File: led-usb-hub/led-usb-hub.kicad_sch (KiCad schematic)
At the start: 142 parts, among them J1 USBC_USB2.0, J2 RGBUSB_54-00266, J3 RGBUSB_54-00266, J4 RGBUSB_54-00266, J5 SWD, SW1 RESET, SW2 BOOLSEL, SW3 LED_EN, U1 RP2040, U10 TPD2EUSB30, U11 TPD2EUSB30, U12 TC54VN3002, U13 W25Q16JVSN, U2 TPS2042D, U3 TPS2042D, U4 TPS563257DRLR, U5 TPS563257DRLR, U6 TUSB2046IBVF, U7 TPD2EUSB30, U8 TPD2EUSB30, U9 TPD2EUSB30, Y1 12Mhz, Y2 6Mhz

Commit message: Even more goddamn clean up and closer placement of decoupling caps
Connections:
- net EN_LED: now also U1.31 (GPIO20); no longer U1.32 (GPIO21)
- net LED_PWR: now also U1.36 (GPIO24); no longer U1.37 (GPIO25)
- net LED_USB: now also U1.35 (GPIO23); no longer U1.36 (GPIO24)
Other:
- moved on the sheet: R52, SW3
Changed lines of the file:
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@@
   (junction (at 33.02 82.55) (diameter 0) (color 0 0 0 0)
   )
-  (junction (at 299.72 243.84) (diameter 0) (color 0 0 0 0)
+  (junction (at 299.72 241.3) (diameter 0) (color 0 0 0 0)
   )
   (junction (at 158.75 146.05) (diameter 0) (color 0 0 0 0)
@@
   (no_connect (at 281.94 210.82))
   (no_connect (at 281.94 236.22))
-  (no_connect (at 281.94 248.92))
+  (no_connect (at 281.94 254))
   (no_connect (at 247.65 90.17))
   (no_connect (at 281.94 208.28))
-  (no_connect (at 281.94 241.3))
+  (no_connect (at 281.94 243.84))
   (bus_entry (at 360.68 199.39) (size -2.54 2.54)
     (stroke (width 0) (type default))
@@
     (stroke (width 0) (type default))
   )
-  (wire (pts (xy 299.72 243.84) (xy 304.8 243.84))
+  (wire (pts (xy 299.72 241.3) (xy 304.8 241.3))
     (stroke (width 0) (type default))
   )
@@
     (stroke (width 0) (type default))
   )
-  (wire (pts (xy 281.94 243.84) (xy 299.72 243.84))
+  (wire (pts (xy 281.94 241.3) (xy 299.72 241.3))
     (stroke (width 0) (type default))
   )
@@
     (stroke (width 0) (type default))
   )
-  (wire (pts (xy 284.48 254) (xy 281.94 254))
+  (wire (pts (xy 284.48 251.46) (xy 281.94 251.46))
     (stroke (width 0) (type default))
   )
@@
     (stroke (width 0) (type default))
   )
-  (wire (pts (xy 299.72 241.3) (xy 299.72 243.84))
+  (wire (pts (xy 299.72 238.76) (xy 299.72 241.3))
     (stroke (width 0) (type default))
   )
@@
     (stroke (width 0) (type default))
   )
-  (wire (pts (xy 299.72 233.68) (xy 299.72 231.14))
+  (wire (pts (xy 299.72 231.14) (xy 299.72 228.6))
     (stroke (width 0) (type default))
   )
@@
     (stroke (width 0) (type default))
   )
-  (wire (pts (xy 284.48 251.46) (xy 281.94 251.46))
+  (wire (pts (xy 284.48 248.92) (xy 281.94 248.92))
     (stroke (width 0) (type default))
   )
@@
     (stroke (width 0) (type default))
   )
-  (wire (pts (xy 314.96 243.84) (xy 320.04 243.84))
+  (wire (pts (xy 314.96 241.3) (xy 320.04 241.3))
     (stroke (width 0) (type default))
   )
@@
     (stroke (width 0) (type default))
   )
-  (wire (pts (xy 320.04 243.84) (xy 320.04 247.65))
+  (wire (pts (xy 320.04 241.3) (xy 320.04 245.11))
     (stroke (width 0) (type default))
   )
@@
     (effects (font (size 1.27 1.27) (color 0 0 194 0)) (justify right bottom))
   )
-  (label "EN_LED" (at 299.72 243.84 180) (fields_autoplaced)
+  (label "EN_LED" (at 299.72 241.3 180) (fields_autoplaced)
     (effects (font (size 1.27 1.27) (color 0 0 194 0)) (justify right bottom))
   )
@@
     )
   )
-  (global_label "LED_USB" (shape output) (at 284.48 251.46 0) (fields_autoplaced)
+  (global_label "LED_USB" (shape output) (at 284.48 248.92 0) (fields_autoplaced)
     (effects (font (size 1.27 1.27)) (justify left))
-    (property "Intersheetrefs" "${INTERSHEET_REFS}" (at 295.6105 251.46 0)
+    (property "Intersheetrefs" "${INTERSHEET_REFS}" (at 295.6105 248.92 0)
       (effects (font (size 1.27 1.27)) (justify left) hide)
     )
@@
     )
   )
-  (global_label "LED_PWR" (shape output) (at 284.48 254 0) (fields_autoplaced)
+  (global_label "LED_PWR" (shape output) (at 284.48 251.46 0) (fields_autoplaced)
     (effects (font (size 1.27 1.27)) (justify left))
-    (property "Intersheetrefs" "${INTERSHEET_REFS}" (at 295.7919 254 0)
+    (property "Intersheetrefs" "${INTERSHEET_REFS}" (at 295.7919 251.46 0)
       (effects (font (size 1.27 1.27)) (justify left) hide)
     )
@@
     )
   )
-  (symbol (lib_id "Switch:SW_Push") (at 309.88 243.84 0) (unit 1)
+  (symbol (lib_id "Switch:SW_Push") (at 309.88 241.3 0) (unit 1)
     (in_bom yes) (on_board yes) (dnp no)
-    (property "Reference" "SW3" (at 309.88 246.38 0)
+    (property "Reference" "SW3" (at 309.88 243.84 0)
       (effects (font (size 1.27 1.27)))
     )
-    (property "Value" "LED_EN" (at 309.88 248.92 0)
+    (property "Value" "LED_EN" (at 309.88 246.38 0)
       (effects (font (size 1.27 1.27)))
     )
-    (property "Footprint" "KSS221GLFS:SW_KSS221GLFS" (at 309.88 238.76 0)
+    (property "Footprint" "KSS221GLFS:SW_KSS221GLFS" (at 309.88 236.22 0)
       (effects (font (size 1.27 1.27)) hide)
     )
-    (property "Datasheet" "~" (at 309.88 238.76 0)
+    (property "Datasheet" "~" (at 309.88 236.22 0)
       (effects (font (size 1.27 1.27)) hide)
     )
@@
     )
   )
-  (symbol (lib_id "power:Earth") (at 320.04 247.65 0) (unit 1)
+  (symbol (lib_id "power:Earth") (at 320.04 245.11 0) (unit 1)
     (in_bom yes) (on_board yes) (dnp no) (fields_autoplaced)
-    (property "Reference" "#PWR045" (at 320.04 254 0)
+    (property "Reference" "#PWR045" (at 320.04 251.46 0)
       (effects (font (size 1.27 1.27)) hide)
     )
-    (property "Value" "Earth" (at 320.04 251.46 0)
+    (property "Value" "Earth" (at 320.04 248.92 0)
       (effects (font (size 1.27 1.27)) hide)
     )
-    (property "Footprint" "" (at 320.04 247.65 0)
+    (property "Footprint" "" (at 320.04 245.11 0)
       (effects (font (size 1.27 1.27)) hide)
     )
-    (property "Datasheet" "~" (at 320.04 247.65 0)
+    (property "Datasheet" "~" (at 320.04 245.11 0)
       (effects (font (size 1.27 1.27)) hide)
     )
@@
     )
   )
-  (symbol (lib_id "power:+3V3_PI") (at 299.72 231.14 0) (unit 1)
+  (symbol (lib_id "power:+3V3_PI") (at 299.72 228.6 0) (unit 1)
     (in_bom yes) (on_board yes) (dnp no) (fields_autoplaced)
-    (property "Reference" "#PWR065" (at 299.72 234.95 0)
+    (property "Reference" "#PWR065" (at 299.72 232.41 0)
       (effects (font (size 1.27 1.27)) hide)
     )
-    (property "Value" "+3V3_PI" (at 299.72 227.33 0)
+    (property "Value" "+3V3_PI" (at 299.72 224.79 0)
       (effects (font (size 1.27 1.27)))
     )
-    (property "Footprint" "" (at 299.72 231.14 0)
+    (property "Footprint" "" (at 299.72 228.6 0)
       (effects (font (size 1.27 1.27)) hide)
     )
-    (property "Datasheet" "" (at 299.72 231.14 0)
+    (property "Datasheet" "" (at 299.72 228.6 0)
       (effects (font (size 1.27 1.27)) hide)
     )
@@
     )
   )
-  (symbol (lib_id "Device:R_US") (at 299.72 237.49 0) (unit 1)
+  (symbol (lib_id "Device:R_US") (at 299.72 234.95 0) (unit 1)
     (in_bom yes) (on_board yes) (dnp no)
-    (property "Reference" "R52" (at 301.625 236.22 0)
+    (property "Reference" "R52" (at 301.625 233.68 0)
       (effects (font (size 1.27 1.27)) (justify left))
     )
-    (property "Value" "10k" (at 301.625 238.76 0)
+    (property "Value" "10k" (at 301.625 236.22 0)
       (effects (font (size 1.27 1.27)) (justify left))
     )
-    (property "Footprint" "Resistor_SMD:R_0603_1608Metric" (at 300.736 237.744 90)
+    (property "Footprint" "Resistor_SMD:R_0603_1608Metric" (at 300.736 235.204 90)
       (effects (font (size 1.27 1.27)) hide)
     )
-    (property "Datasheet" "~" (at 299.72 237.49 0)
+    (property "Datasheet" "~" (at 299.72 234.95 0)
       (effects (font (size 1.27 1.27)) hide)
     )

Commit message: Clean up and aligning
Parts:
- D1: value ORANGE (PWR) -> PWR; Color (none) -> Orange
- D2: value GREEN (USB) -> USB; Color (none) -> Green
- SW3: value LED_EN -> LED EN
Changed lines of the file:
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@@
     (effects (font (size 1.27 1.27) (color 0 0 255 0)) (justify left bottom))
   )
-  (label "LED_USB'" (at 370.84 243.84 0) (fields_autoplaced)
-    (effects (font (size 1.27 1.27) (color 0 0 255 0)) (justify left bottom))
+  (label "LED_USB'" (at 372.11 243.84 270) (fields_autoplaced)
+    (effects (font (size 1.27 1.27) (color 0 0 255 0)) (justify right bottom))
   )
   (label "CC1" (at 46.99 31.75 0) (fields_autoplaced)
@@
     (effects (font (size 1.27 1.27) (color 0 0 255 0)) (justify left bottom))
   )
-  (label "LED_PWR'" (at 370.84 237.49 0) (fields_autoplaced)
+  (label "LED_PWR'" (at 372.11 237.49 90) (fields_autoplaced)
     (effects (font (size 1.27 1.27) (color 0 0 255 0)) (justify left bottom))
   )
@@
       (effects (font (size 1.27 1.27)))
     )
-    (property "Value" "LED_EN" (at 309.88 246.38 0)
+    (property "Value" "LED EN" (at 309.88 246.38 0)
       (effects (font (size 1.27 1.27)))
     )
@@
   (symbol (lib_id "Device:LED") (at 379.73 237.49 180) (unit 1)
     (in_bom yes) (on_board yes) (dnp no)
-    (property "Reference" "D1" (at 379.73 231.14 0)
+    (property "Reference" "D1" (at 379.73 232.41 0)
       (effects (font (size 1.27 1.27)))
     )
-    (property "Value" "ORANGE (PWR)" (at 379.73 233.68 0)
+    (property "Value" "PWR" (at 379.73 234.95 0)
       (effects (font (size 1.27 1.27)))
     )
@@
       (effects (font (size 1.27 1.27)) hide)
     )
+    (property "Color" "Orange" (at 379.73 239.395 0)
+      (effects (font (size 1.27 1.27) italic))
+    )
     (pin "1")
     (pin "2")
@@
   (symbol (lib_id "Device:LED") (at 379.73 243.84 180) (unit 1)
     (in_bom yes) (on_board yes) (dnp no)
-    (property "Reference" "D2" (at 379.73 247.015 0)
+    (property "Reference" "D2" (at 379.73 246.38 0)
       (effects (font (size 1.27 1.27)))
     )
-    (property "Value" "GREEN (USB)" (at 379.73 249.555 0)
+    (property "Value" "USB" (at 379.73 248.285 0)
       (effects (font (size 1.27 1.27)))
     )
@@
       (effects (font (size 1.27 1.27)) hide)
     )
+    (property "Color" "Green" (at 379.73 250.19 0)
+      (effects (font (size 1.27 1.27) italic))
+    )
     (pin "1")

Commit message: Pick better LED resistor values
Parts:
- R10, R4, R7: value 30 -> 62
- R11, R5, R8: value 30 -> 27
- R3, R6, R9: value 130 -> 200
- R53: value 300 -> 2k
- R54: value 300 -> 2.4k
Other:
- note added: "Blue USB (200 mcd): Ave 350cd@20mA Vf=0.3V, Target Current: ~11.5mA Resistance: 27Ω"
- note added: "Green Indicator (2.5 mcd): 90mcd@20mA Vf=1.3V, Target Current: ~0.55mA Resistance: 2.4kΩ"
- note added: "Green USB (200 mcd): Ave 800cd@20mA Vf=0.3V, Target Current: ~5mA Resistance: 62Ω"
- note added: "LED Resistor Selection"
- note added: "Orange Indicator (2.5 mcd): Ave 77mcd@20mA (curve compensating) Vf=1.3V, Target Current: ~0.65mA Resistance: 2kΩ"
- note added: "Red USB (200 mcd): Ave 600cd@20mA Vf=1.3V, Target Current: ~6.5mA Resistance: 200Ω"
- note added: "Target is brightness of 2.5 mcd"
- note added: "Target is brightness of 200 mcd"
- moved on the sheet: D1, D2, R53, R54, U12

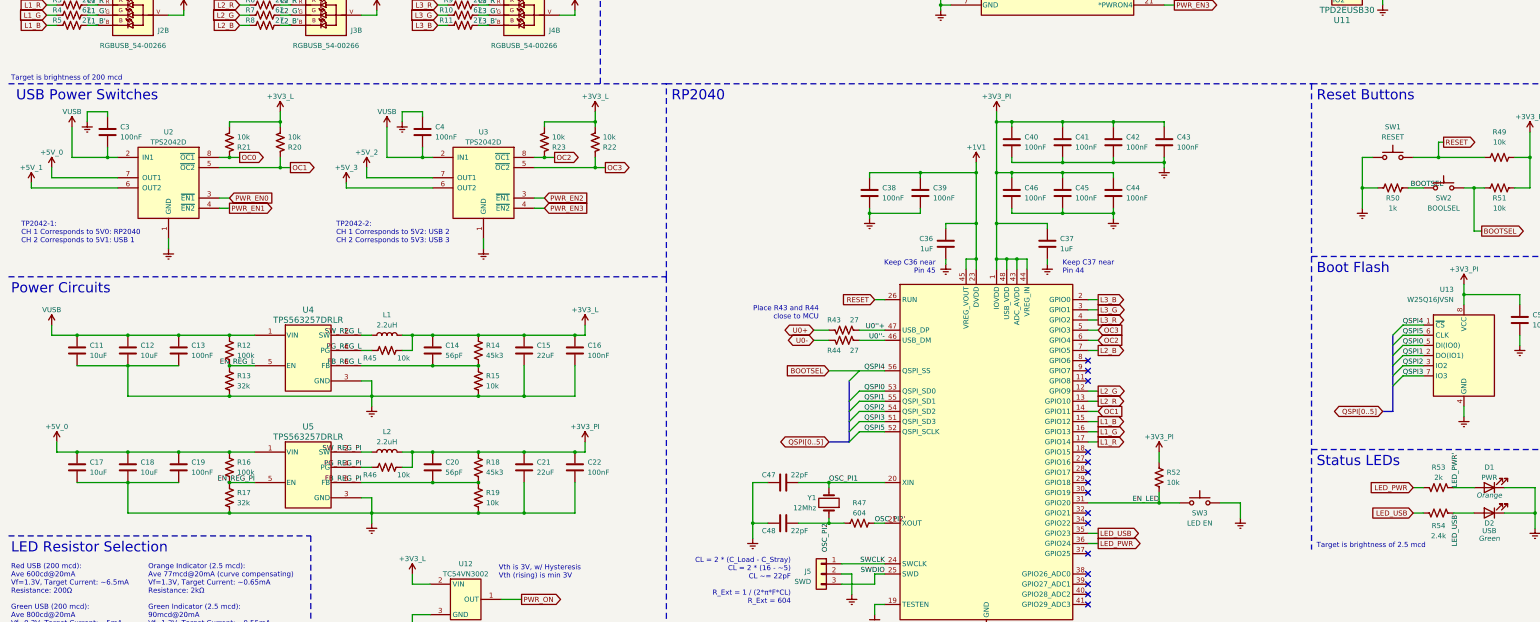
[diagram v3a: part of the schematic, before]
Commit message: Switch 'Brightness' to 'Intensity', more technically correct
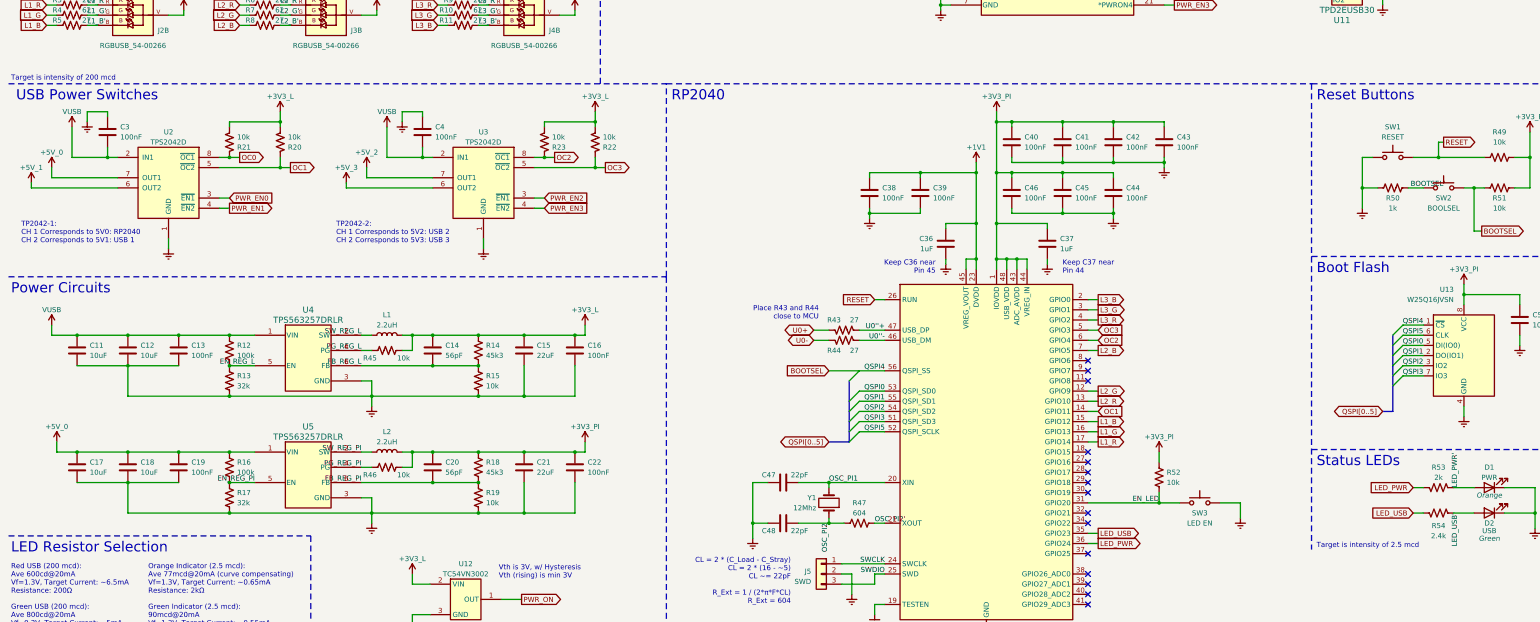
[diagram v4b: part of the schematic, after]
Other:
- note added: "Target is intensity of 2.5 mcd"
- note added: "Target is intensity of 200 mcd"
- note removed: "Target is brightness of 2.5 mcd"
- note removed: "Target is brightness of 200 mcd"
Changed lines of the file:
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@@
     (effects (font (size 2.54 2.54)) (justify left bottom))
   )
-  (text "Target is brightness of 200 mcd" (at 12.7 135.89 0)
+  (text "Target is intensity of 200 mcd" (at 12.7 135.89 0)
     (effects (font (size 1.27 1.27)) (justify left bottom))
   )
@@
     (effects (font (size 2.54 2.54)) (justify left bottom))
   )
-  (text "Target is brightness of 2.5 mcd" (at 339.09 252.73 0)
+  (text "Target is intensity of 2.5 mcd" (at 339.09 252.73 0)
     (effects (font (size 1.27 1.27)) (justify left bottom))
   )

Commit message: Final pass on components and layout V2 Ordering will happen soon
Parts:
- R51: value 10k -> 10k (DNF)
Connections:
- net +3V3_L: now also U12.3 (VIN); no longer U12.2 (VIN)
- net Earth: now also U12.2 (GND); no longer U12.3 (GND)
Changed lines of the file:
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@@
   (junction (at 382.27 78.74) (diameter 0) (color 0 0 0 0)
   )
+  (junction (at 41.91 214.63) (diameter 0) (color 0 0 0 0)
+  )
   (junction (at 228.6 63.5) (diameter 0) (color 0 0 0 0)
   )
@@
   (junction (at 275.59 158.75) (diameter 0) (color 0 0 0 0)
   )
+  (junction (at 54.61 243.84) (diameter 0) (color 0 0 0 0)
+  )
   (junction (at 212.09 77.47) (diameter 0) (color 0 0 0 0)
   )
@@
   (junction (at 275.59 168.91) (diameter 0) (color 0 0 0 0)
   )
+  (junction (at 54.61 214.63) (diameter 0) (color 0 0 0 0)
+  )
   (junction (at 389.89 78.74) (diameter 0) (color 0 0 0 0)
   )
@@
   (junction (at 254 180.34) (diameter 0) (color 0 0 0 0)
   )
-  (junction (at 41.91 236.22) (diameter 0) (color 0 0 0 0)
-  )
   (junction (at 264.16 46.99) (diameter 0) (color 0 0 0 0)
   )
@@
   (junction (at 261.62 180.34) (diameter 0) (color 0 0 0 0)
   )
-  (junction (at 41.91 207.01) (diameter 0) (color 0 0 0 0)
-  )
   (junction (at 355.6 68.58) (diameter 0) (color 0 0 0 0)
   )
@@
   (junction (at 46.99 39.37) (diameter 0) (color 0 0 0 0)
   )
+  (junction (at 41.91 243.84) (diameter 0) (color 0 0 0 0)
+  )
   (no_connect (at 46.99 57.15))
   (no_connect (at 46.99 54.61))
@@
     (stroke (width 0.25) (type dash))
   )
-  (wire (pts (xy 29.21 236.22) (xy 41.91 236.22))
+  (wire (pts (xy 29.21 243.84) (xy 41.91 243.84))
     (stroke (width 0) (type default))
   )
@@
     (stroke (width 0) (type default))
   )
-  (wire (pts (xy 41.91 236.22) (xy 54.61 236.22))
+  (wire (pts (xy 41.91 243.84) (xy 54.61 243.84))
     (stroke (width 0) (type default))
   )
@@
     (stroke (width 0) (type default))
   )
-  (wire (pts (xy 41.91 207.01) (xy 54.61 207.01))
+  (wire (pts (xy 41.91 214.63) (xy 54.61 214.63))
     (stroke (width 0) (type default))
   )
@@
     (stroke (width 0) (type default))
   )
+  (wire (pts (xy 29.21 243.84) (xy 29.21 236.22))
+    (stroke (width 0) (type default))
+  )
   (wire (pts (xy 156.21 226.06) (xy 156.21 228.6))
     (stroke (width 0) (type default))
@@
     (stroke (width 0) (type default))
   )
-  (wire (pts (xy 67.31 214.63) (xy 41.91 214.63))
+  (wire (pts (xy 67.31 214.63) (xy 54.61 214.63))
     (stroke (width 0) (type default))
   )
@@
     (stroke (width 0) (type default))
   )
+  (wire (pts (xy 41.91 214.63) (xy 41.91 207.01))
+    (stroke (width 0) (type default))
+  )
   (bus (pts (xy 355.6 218.44) (xy 358.14 218.44))
     (stroke (width 0) (type default))
   )
-  (wire (pts (xy 29.21 207.01) (xy 41.91 207.01))
+  (wire (pts (xy 29.21 214.63) (xy 41.91 214.63))
     (stroke (width 0) (type default))
   )
@@
     (stroke (width 0) (type default))
   )
-  (wire (pts (xy 41.91 214.63) (xy 41.91 207.01))
-    (stroke (width 0) (type default))
-  )
   (wire (pts (xy 33.02 88.9) (xy 30.48 88.9))
     (stroke (width 0) (type default))
@@
     (stroke (width 0) (type default))
   )
+  (wire (pts (xy 54.61 214.63) (xy 54.61 207.01))
+    (stroke (width 0) (type default))
+  )
   (wire (pts (xy 102.87 240.03) (xy 102.87 243.84))
     (stroke (width 0) (type default))
@@
     (stroke (width 0) (type default))
   )
-  (wire (pts (xy 67.31 243.84) (xy 41.91 243.84))
+  (wire (pts (xy 67.31 243.84) (xy 54.61 243.84))
     (stroke (width 0) (type default))
   )
@@
     (stroke (width 0) (type default))
   )
+  (wire (pts (xy 54.61 243.84) (xy 54.61 236.22))
+    (stroke (width 0) (type default))
+  )
   (wire (pts (xy 288.29 170.18) (xy 288.29 168.91))
     (stroke (width 0) (type default))
@@
     (stroke (width 0) (type default))
   )
+  (wire (pts (xy 29.21 214.63) (xy 29.21 207.01))
+    (stroke (width 0) (type default))
+  )
   (wire (pts (xy 382.27 55.88) (xy 382.27 58.42))
     (stroke (width 0) (type default))
@@
     )
   )
-  (global_label "PWR_EN1" (shape output) (at 67.31 167.64 0) (fields_autoplaced)
+  (global_label "PWR_EN1" (shape input) (at 67.31 167.64 0) (fields_autoplaced)
     (effects (font (size 1.27 1.27)) (justify left))
     (property "Intersheetrefs" "${INTERSHEET_REFS}" (at 78.8638 167.64 0)
@@
       (effects (font (size 1.27 1.27)))
     )
-    (property "Value" "10k" (at 384.81 167.64 90)
+    (property "Value" "10k (DNF)" (at 384.81 167.64 90) (do_not_autoplace)
       (effects (font (size 1.27 1.27)))
     )

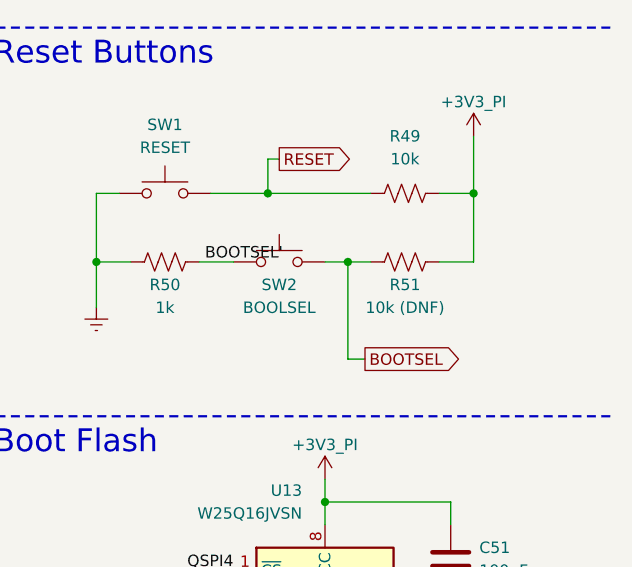
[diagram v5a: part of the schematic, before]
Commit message: Update Bom and DNP mark
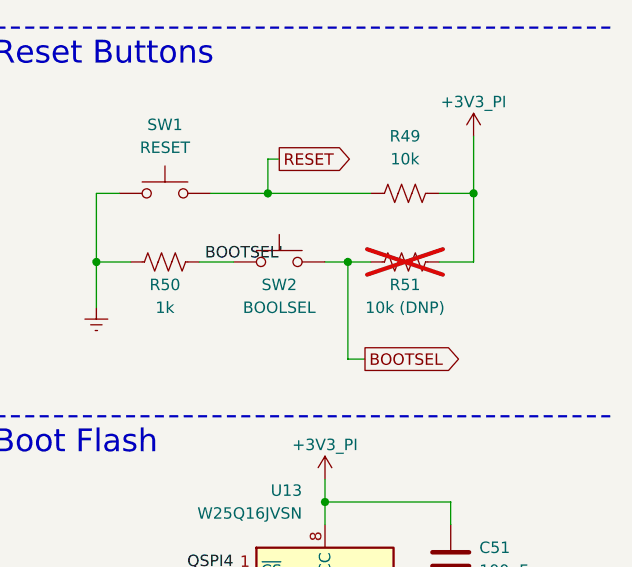
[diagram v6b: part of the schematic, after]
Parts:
- R51: value 10k (DNF) -> 10k (DNP); now not fitted
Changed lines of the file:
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@@
   )
   (symbol (lib_id "Device:R_US") (at 384.81 162.56 90) (unit 1)
-    (in_bom yes) (on_board yes) (dnp no)
+    (in_bom yes) (on_board yes) (dnp yes)
     (property "Reference" "R51" (at 384.81 165.1 90)
       (effects (font (size 1.27 1.27)))
     )
-    (property "Value" "10k (DNF)" (at 384.81 167.64 90) (do_not_autoplace)
+    (property "Value" "10k (DNP)" (at 384.81 167.64 90) (do_not_autoplace)
       (effects (font (size 1.27 1.27)))
     )

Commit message: Fix hole size in PCB
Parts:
- H1, H2, H3, H4: footprint MountingHole:MountingHole_3mm -> MountingHole:MountingHole_4mm
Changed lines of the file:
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@@
       (effects (font (size 1.27 1.27)) (justify left))
     )
-    (property "Footprint" "MountingHole:MountingHole_3mm" (at 138.43 24.13 0)
+    (property "Footprint" "MountingHole:MountingHole_4mm" (at 138.43 24.13 0)
       (effects (font (size 1.27 1.27)) hide)
     )
@@
       (effects (font (size 1.27 1.27)) (justify left))
     )
-    (property "Footprint" "MountingHole:MountingHole_3mm" (at 116.84 31.75 0)
+    (property "Footprint" "MountingHole:MountingHole_4mm" (at 116.84 31.75 0)
       (effects (font (size 1.27 1.27)) hide)
     )
@@
       (effects (font (size 1.27 1.27)) (justify left))
     )
-    (property "Footprint" "MountingHole:MountingHole_3mm" (at 116.84 24.13 0)
+    (property "Footprint" "MountingHole:MountingHole_4mm" (at 116.84 24.13 0)
       (effects (font (size 1.27 1.27)) hide)
     )
@@
       (effects (font (size 1.27 1.27)) (justify left))
     )
-    (property "Footprint" "MountingHole:MountingHole_3mm" (at 138.43 31.75 0)
+    (property "Footprint" "MountingHole:MountingHole_4mm" (at 138.43 31.75 0)
       (effects (font (size 1.27 1.27)) hide)
     )
